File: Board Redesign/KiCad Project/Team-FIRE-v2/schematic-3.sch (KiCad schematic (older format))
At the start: 27 parts, among them IC1 MCP1826T-3302E_DC, IC2 BTS500601TEAAUMA2, J10 PCB.MMCX.F.ST.SMT.JACK.HT, J6 Conn_01x03, J7 Conn_01x03, J8 Conn_01x02, U8 TPS82140

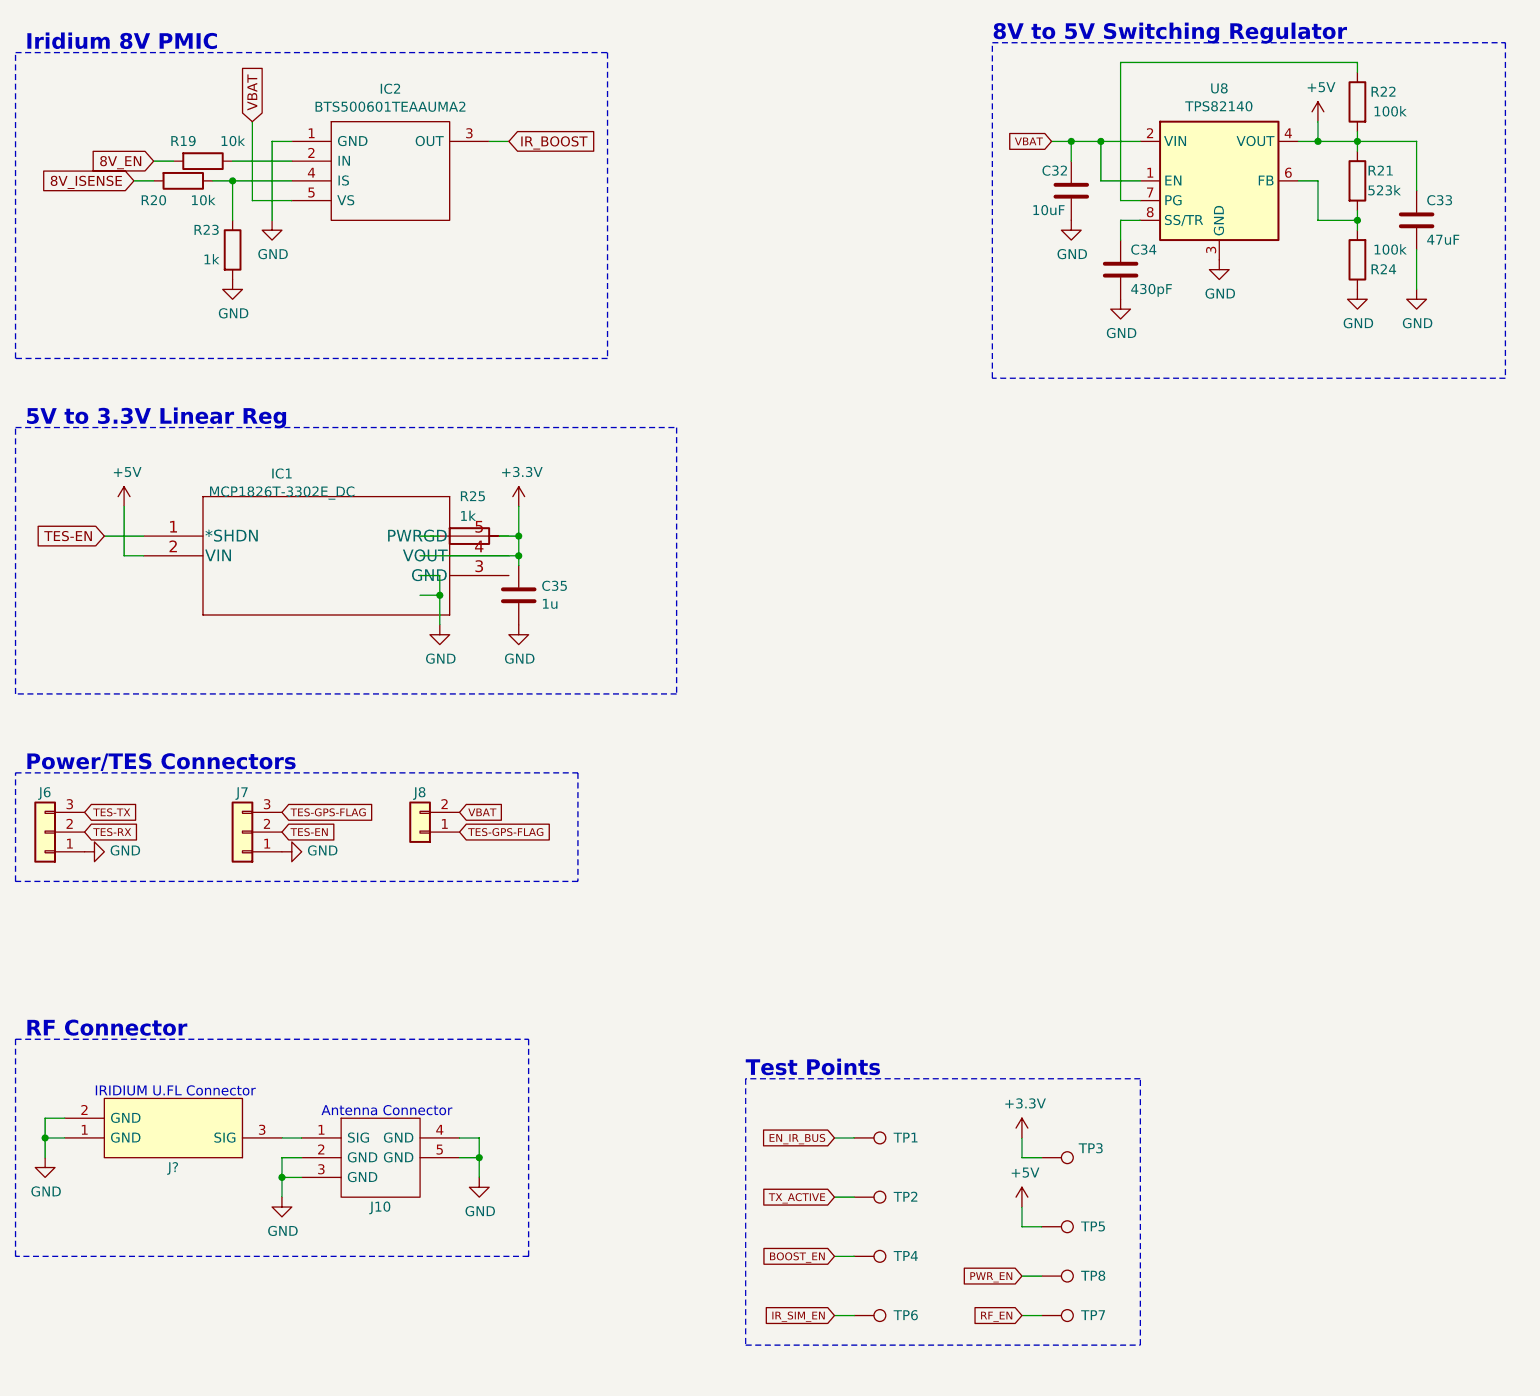
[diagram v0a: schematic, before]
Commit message: Labelled finished sections on schematic, picked LEDs
- Labelled all finished schematic sections if they've been part-selected / verified (and by whom)
- Selected the four debug LEDs and filled out BOM info
- Filled out info for Power/TES connectors
- Filled out info for RF connector
- Filled out info for 5 to 3.3V regulator
- Filled out info for 8 to 5V switching regulator
- Assigned footprints to test points
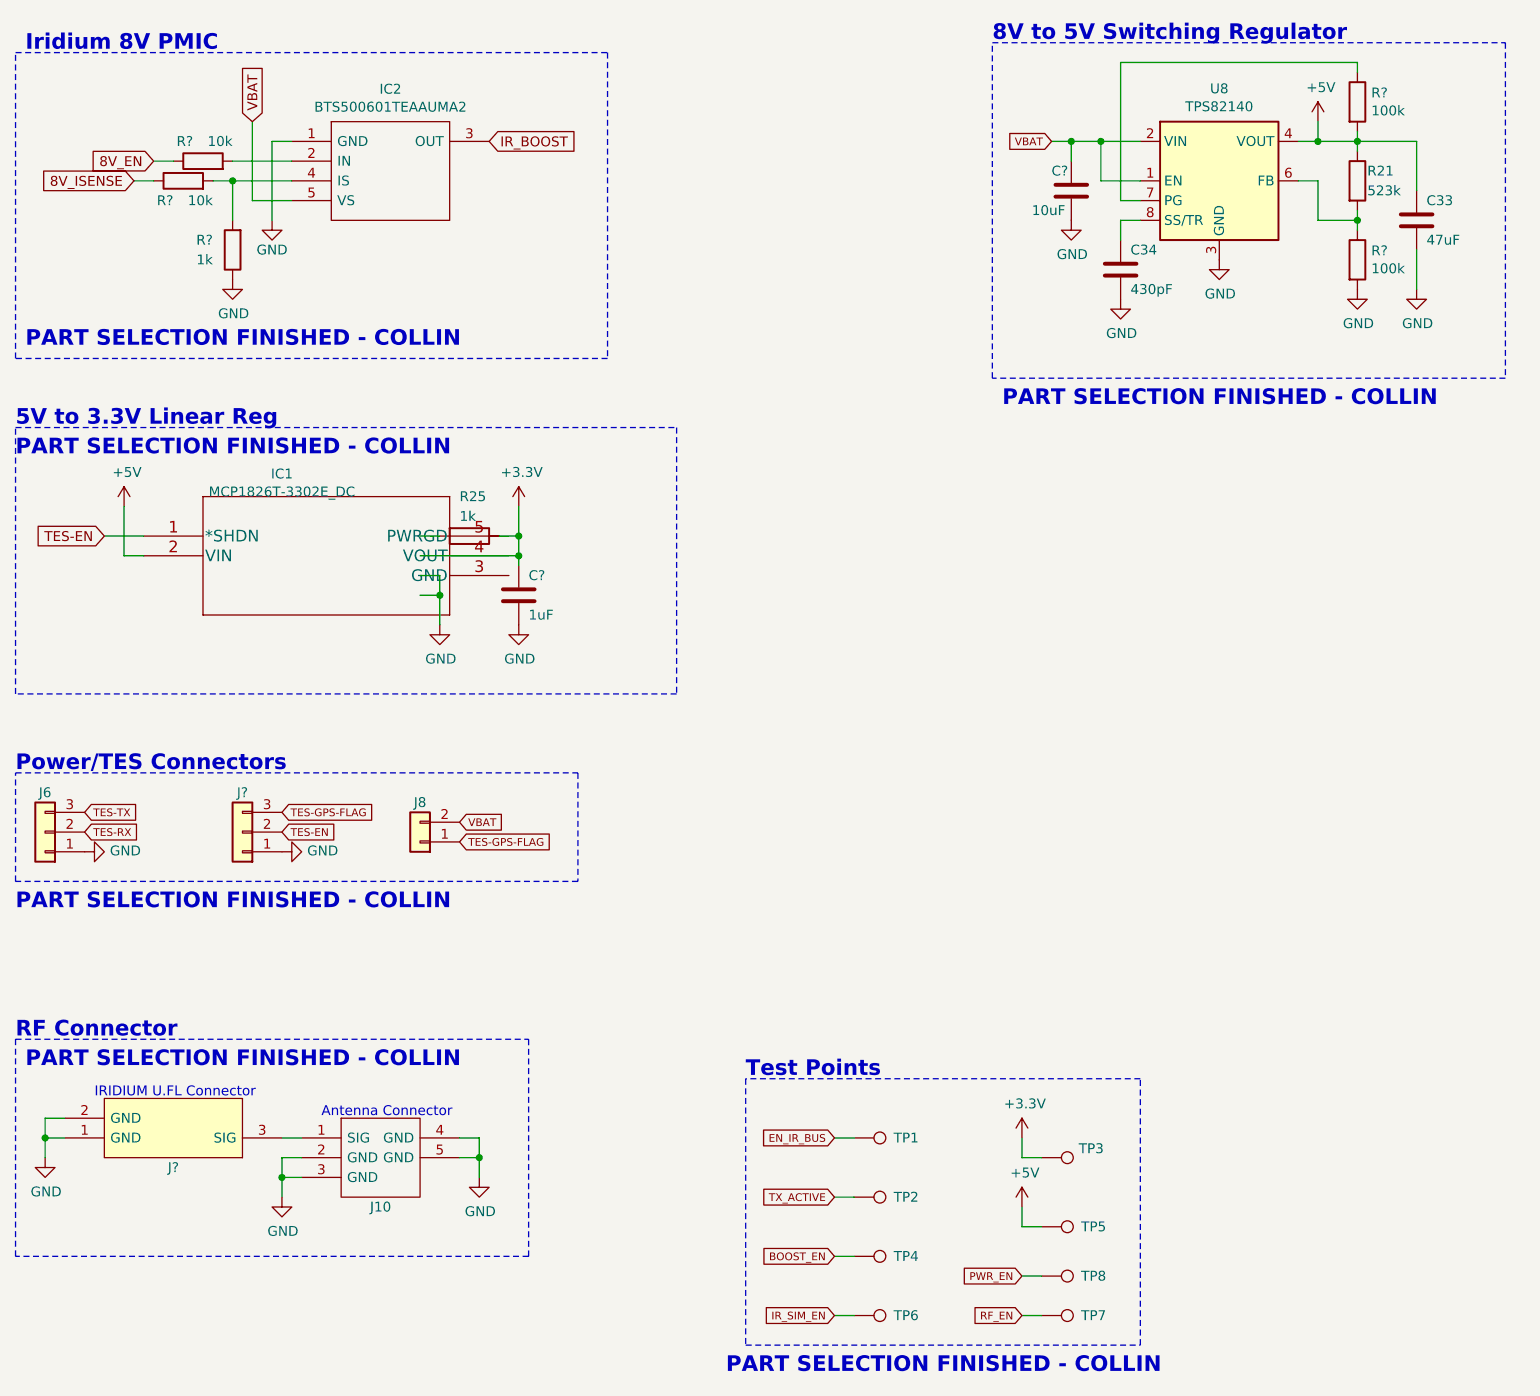
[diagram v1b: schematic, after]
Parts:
- removed C32: 10uF, Capacitor_SMD:C_0805_2012Metric, symbol Device:C
- removed C35: 1u, Capacitor_SMD:C_0805_2012Metric, symbol Device:C
- removed J7: Conn_01x03, Connector_JST:JST_SH_SM03B-SRSS-TB_1x03-1MP_P1.00mm_Horizontal, symbol Connector_Generic:Conn_01x03
- removed R19, R20: 10k, Resistor_SMD:R_0603_1608Metric, symbol Device:R
- removed R22, R24: 100k, Resistor_SMD:R_0603_1608Metric, symbol Device:R
- removed R23: 1k, Resistor_SMD:R_0603_1608Metric, symbol Device:R
- added C?: 1uF, Capacitor_SMD:C_0603_1608Metric, symbol Device:C
- added C?: 10uF, Capacitor_SMD:C_0603_1608Metric, symbol Device:C
- added J?: Conn_01x03, Connector_JST:JST_SH_SM03B-SRSS-TB_1x03-1MP_P1.00mm_Horizontal, symbol Connector_Generic:Conn_01x03
- added R?: 1k, Resistor_SMD:R_0603_1608Metric, symbol Device:R
- added R? (x2): 10k, Resistor_SMD:R_0603_1608Metric, symbol Device:R
- added R? (x2): 100k, Resistor_SMD:R_0603_1608Metric, symbol Device:R
- C33: Link (none) -> https://www.mouser.com/ProductDetail/Taiyo-Yuden/JMK107BBJ4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; MPN (none) -> JMK107BBJ476MA-RE; Manufacturer (none) -> Taiyo Yuden; Qualification (none) -> AEC-Q200; Supplier (none) -> Mouser; Supplier PN (none) -> 963-JMK107BBJ476MARE; Tolerance (none) -> 20%; Type (none) -> Ceramic X5R Capacitor; Voltage Rating (none) -> 6.3 VDC
- C34: footprint Capacitor_SMD:C_0805_2012Metric -> Capacitor_SMD:C_0603_1608Metric; Link (none) -> https://www.mouser.com/ProductDetail/AVX/06035C431JAT2A?qs=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; MPN (none) -> 06035C431JAT2A; Manufacturer (none) -> AVX; Supplier (none) -> Mouser; Supplier PN (none) -> 581-06035C431JAT2A; Tolerance (none) -> 5%; Type (none) -> Ceramic X7R Capacitor; Voltage Rating (none) -> 50 VDC
- J6: Description (none) -> TES TX/RX Header; Link (none) -> https://www.digikey.ca/product-detail/en/jst-sales-america-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; Manufacturer (none) -> JST Sales America Inc.; Supplier (none) -> Digikey; Supplier PN (none) -> 455-1803-1-ND
- J8: Description (none) -> TES VBAT/TES-GPS Header; Link (none) -> https://www.digikey.ca/product-detail/en/molex/0436500200/W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; Supplier (none) -> Mouser; Supplier PN (none) -> WM1860-ND
- J?: Height 1.25 -> (none); Link (none) -> https://www.mouser.com/ProductDetail/Hirose-Connector/UFL-R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; MPN (none) -> U.FL-R-SMT(10); Manufacturer (none) -> Hirose; Manufacturer_Name Hirose -> (none); Manufacturer_Part_Number U.FL-R-SMT(10) -> (none); Mouser Part Number 798-U.FL-R-SMT10 -> (none); Mouser Price/Stock https://www.mouser.com/Search/Refine.aspx?Keyword=798-U.FL-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 -> (none); Supplier (none) -> Mouser; Supplier PN (none) -> 798-U.FL-R-SMT10
- R21: footprint Resistor_SMD:R_0603_1608Metric -> Resistor_SMD:R_0805_2012Metric; Link (none) -> https://www.mouser.com/ProductDetail/Panasonic/ERJ-PB6D5233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; MPN (none) -> ERJ-PB6D5233V; Qualification (none) -> AEC-Q200; Supplier (none) -> Panasonic; Supplier PN (none) -> 667-ERJ-PB6D5233V; Tolerance (none) -> 0.5%; Type (none) -> Thick Film Resistor; Voltage Ratign (none) -> 150 V
- R25: Link (none) -> https://www.mouser.com/ProductDetail/Vishay-Beyschlag/MCT06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; MPN (none) -> MCT0603MD1001BP500; Manufacturer (none) -> Vishay; Supplier (none) -> Mouser; Supplier PN (none) -> 594-MCT0603MD1001BP5; Tolerance (none) -> 0.1%; Type (none) -> Thin Film Resistor; Voltage Rating (none) -> 75 V
- U8: Current Rating (none) -> 2 A; Description (none) -> 8 to 5V IC switching regulator; Link (none) -> https://www.mouser.com/ProductDetail/Texas-Instruments/TPS8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; MPN (none) -> TPS82140SILR; Manufacturer (none) -> Texas Instruments; Supplier (none) -> Mouser; Supplier PN (none) -> 595-TPS82140SILR; Voltage Rating (none) -> 3 to 17 V
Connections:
- wire segments 72 -> 71
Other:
- note added: "PART SELECTION FINISHED - COLLIN"
- moved on the sheet: J8
